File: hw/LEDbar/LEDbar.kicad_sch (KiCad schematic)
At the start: 25 parts, among them J1 Conn_01x04, J2 Conn_01x04, J3 Conn_01x04, U1 STP16CP05XT

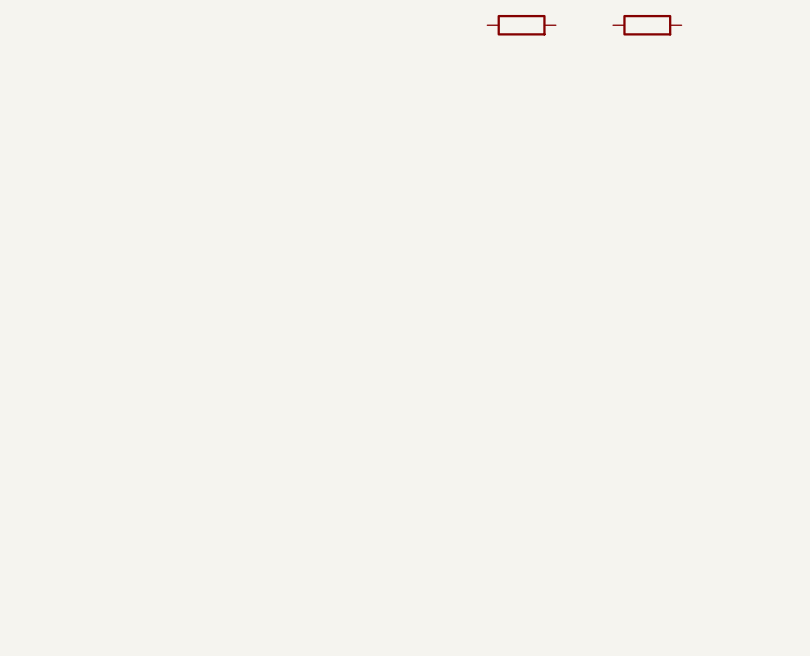
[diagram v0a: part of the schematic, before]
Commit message: first version of the led bar finished
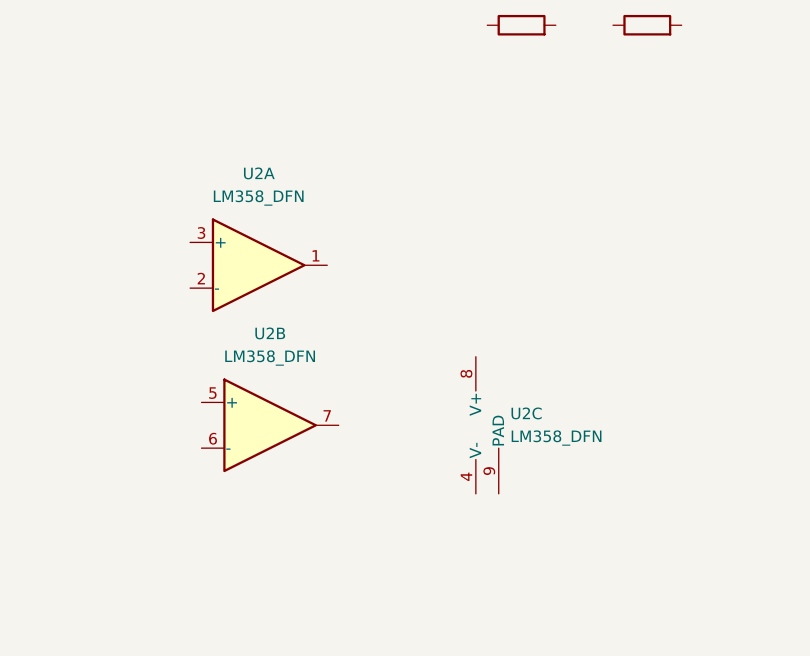
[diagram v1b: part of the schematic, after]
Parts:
- added U2: LM358_DFN, Package_DFN_QFN:DFN-8-1EP_2x2mm_P0.5mm_EP1.05x1.75mm, symbol Amplifier_Operational:LM358_DFN
- BAR1: footprint Display:HDSP-4830 -> Display:HLCP-J100
- C1, C10, C2, C3, C4, C5, C6, C7, C8, C9: footprint Capacitor_SMD:C_0603_1608Metric -> Capacitor_SMD:C_0402_1005Metric
- R1, R10, R2, R3, R4, R5, R6, R7, R8, R9: footprint Resistor_SMD:R_0603_1608Metric -> Resistor_SMD:R_0402_1005Metric
